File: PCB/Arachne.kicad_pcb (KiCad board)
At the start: 2 copper layers, 100 x 100 mm, 276 parts, among them J201 SW2, J301 SW2, J401 SW2, J501 SW2, J601 SW2, J701 SW2, J801 V_IN, J901 USB_B, J902 PROG_CONN_STM_6p, J903 DBG_UART, M201 Stepper_Motor_bipolar, M301 Stepper_Motor_bipolar, M401 Stepper_Motor_bipolar, M501 Stepper_Motor_bipolar, M601 Stepper_Motor_bipolar, M701 Stepper_Motor_bipolar, Q801 AOD4189, SW101 SW_Push, U101 STM32L452CEUx, U102 WS2818B, U201 L6470_HTSSOP28, U301 L6470_HTSSOP28, U401 L6470_HTSSOP28, U501 L6470_HTSSOP28, U601 L6470_HTSSOP28, U701 L6470_HTSSOP28, U801 ACS712xLCTR-20A, U802 NCP1117-5.0_SOT223, U803 L5973D, U804 NCP1117-3.3_SOT223, U901 USBLC6-2SC6

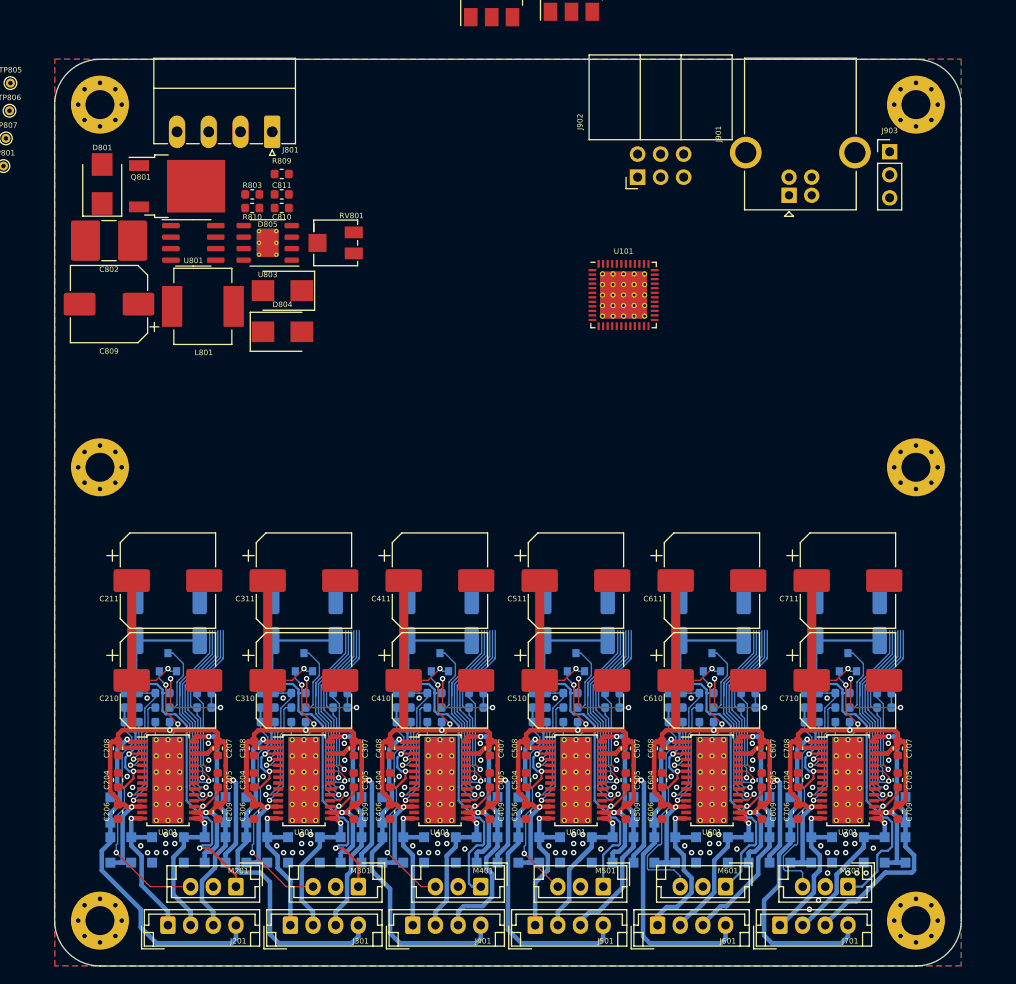
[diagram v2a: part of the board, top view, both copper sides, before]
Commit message: Schema&PCB: shrink board to 80x100mm, remove excessive mounting holes
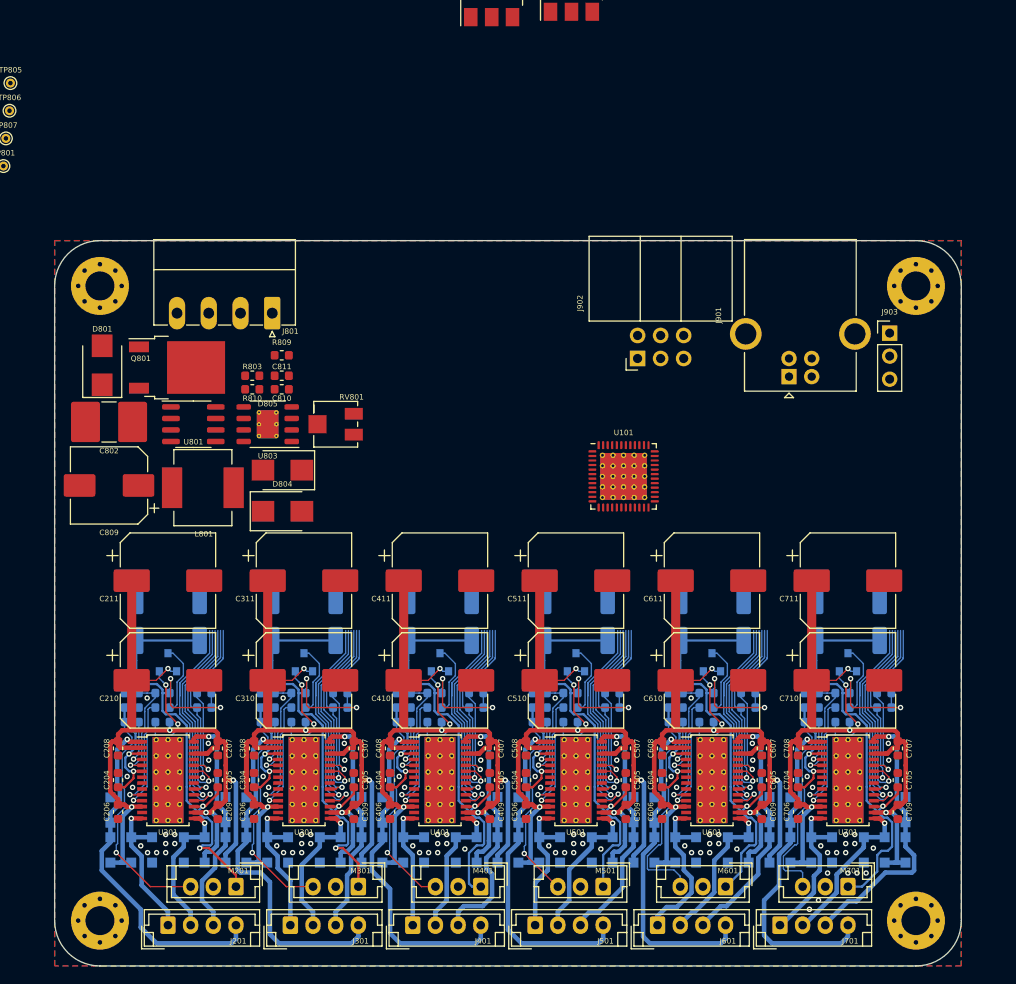
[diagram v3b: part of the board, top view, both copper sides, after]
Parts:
- removed H105, H106: M3, MountingHole:MountingHole_3.2mm_M3_Pad_Via
- moved H101 127.3 mm to (105.0, 145.0)
- moved R809 20.0 mm to (125.0, 82.7)
- moved C802 20.0 mm to (106.0, 90.0)
- moved C809 20.0 mm to (106.0, 97.0)
- moved C810 20.0 mm to (125.0, 86.4)
- moved C811 20.0 mm to (125.0, 84.9)
- moved D801 20.0 mm to (105.2, 83.8)
- moved H102 20.0 mm to (195.0, 75.0)
- moved H103 20.0 mm to (105.0, 75.0)
- moved J801 20.0 mm to (124.0, 78.0)
- moved J901 20.0 mm to (181.0, 85.0)
- moved J902 20.0 mm to (164.3, 83.0)
- moved J903 20.0 mm to (192.1, 80.2)
- moved L801 20.0 mm to (116.3, 97.2)
- moved Q801 20.0 mm to (113.5, 84.0)
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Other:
- board size 100 x 100 mm -> 100 x 80 mm

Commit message: PCB: route bus between drivers, place resistor nets
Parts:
- RN101, RN102, RN103: moved to B.Cu
- moved D104 253.8 mm to (119.0, 115.0), turned to 270 degrees
- moved D102 252.3 mm to (119.0, 122.0), turned to 90 degrees
- moved D103 237.0 mm to (134.0, 115.0), turned to 90 degrees
- moved D101 233.6 mm to (134.0, 122.0), turned to 90 degrees
- moved RN101 229.1 mm to (120.0, 118.0), turned to 270 degrees
- moved RN102 207.9 mm to (150.0, 107.0), turned to 270 degrees
- moved RN103 173.7 mm to (180.0, 107.0), turned to 270 degrees
- moved D105 13.5 mm to (359.5, 52.5), turned to 90 degrees
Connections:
- RN101 pad 5: /BUSY_1 -> /FLAG_2
- RN101 pad 6: /FLAG_1 -> /BUSY_2
- RN101 pad 7: /FLAG_2 -> /FLAG_1
- RN101 pad 8: /BUSY_2 -> /BUSY_1
- RN102 pad 5: /BUSY_3 -> /FLAG_4
- RN102 pad 6: /FLAG_3 -> /BUSY_4
- RN102 pad 7: /FLAG_4 -> /BUSY_3
- RN102 pad 8: /BUSY_4 -> /FLAG_3
- RN103 pad 5: /BUSY_5 -> /FLAG_6
- RN103 pad 6: /FLAG_5 -> /BUSY_6
- RN103 pad 7: /FLAG_6 -> /BUSY_5
- RN103 pad 8: /BUSY_6 -> /FLAG_5
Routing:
- net VMOT: track 546.5 -> 643.0 mm
- net /SPI_MISO: track 154.6 -> 241.3 mm, vias 6 -> 16
- net /SPI_SCK: track 128.5 -> 212.3 mm, vias 6 -> 16
- net /SPI_MOSI: track 128.5 -> 211.3 mm
- net /FLAG_4: track 18.8 -> 15.6 mm
- net /FLAG_2: track 18.8 -> 15.6 mm
- net /FLAG_3: track 18.8 -> 15.7 mm
- net /FLAG_5: track 18.8 -> 15.7 mm
- net /FLAG_1: track 18.8 -> 15.7 mm
- net /FLAG_6: track 18.8 -> 15.8 mm
- net /BUSY_2: track 19.4 -> 16.4 mm
- net /BUSY_4: track 19.4 -> 16.4 mm
- net /BUSY_3: track 19.4 -> 16.4 mm
- net /BUSY_5: track 19.4 -> 16.5 mm
- net /BUSY_6: track 19.4 -> 16.5 mm
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
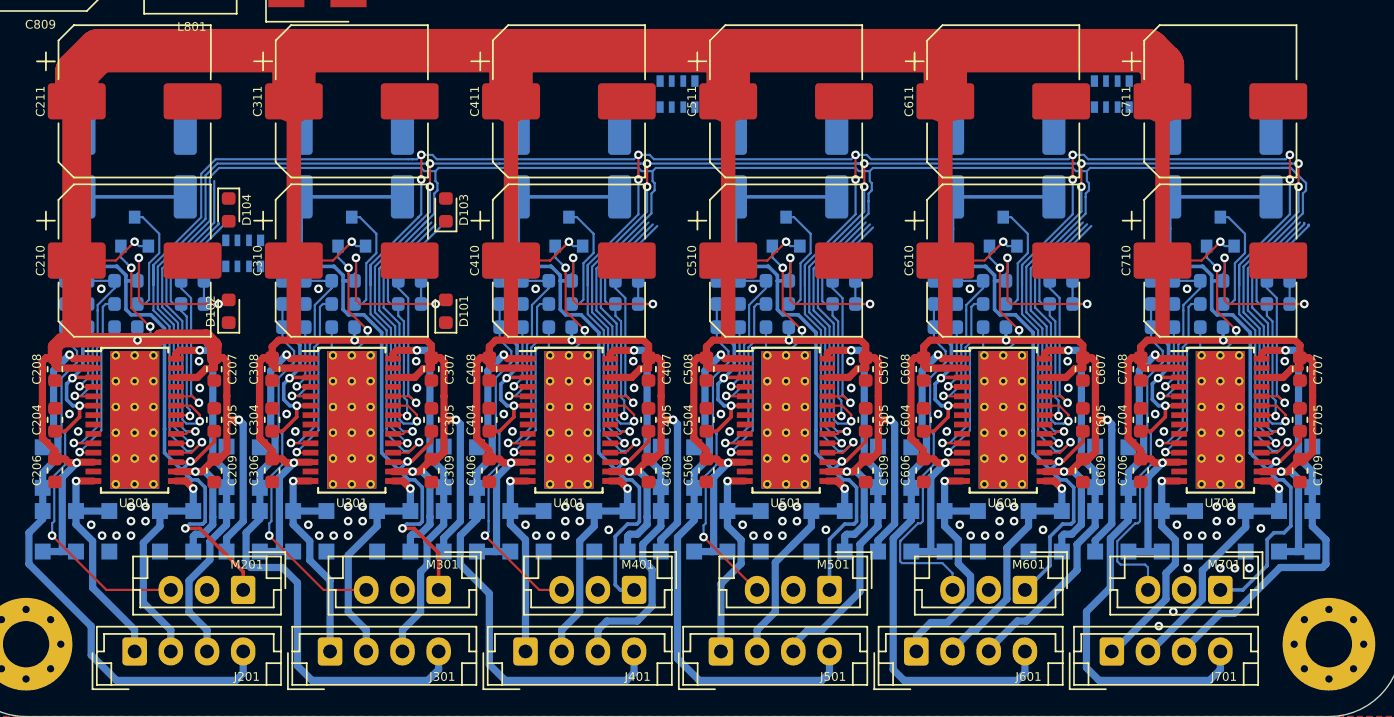
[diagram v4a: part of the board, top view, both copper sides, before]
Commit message: PCB: update VMOT traces to 1 class wider variant
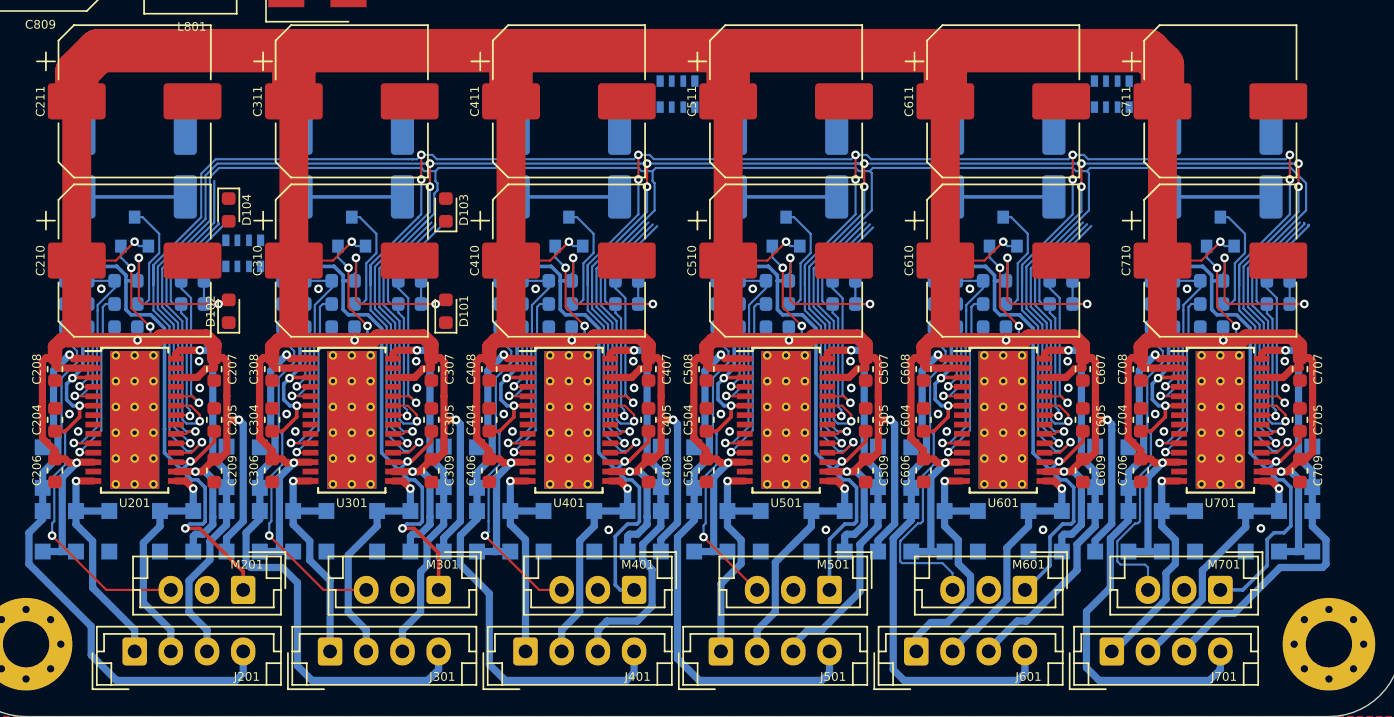
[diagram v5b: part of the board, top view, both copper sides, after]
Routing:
- net +3V3: track 466.6 -> 467.4 mm
- net VMOT: track 643.0 -> 643.9 mm
- net GND: vias 88 -> 34

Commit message: PCB: route current meter, reverse polarity protection, stepdown converter
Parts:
- C802, C804, C805, C810, C811, D803, D804, D805, F801, L901, R801, R802, R804, R805, R808, R809, R810, RV801, U101, U803, U901: moved to B.Cu
- D802: footprint Package_TO_SOT_SMD:SOT-23-6 -> Package_DFN_QFN:ST_UQFN-6L_1.5x1.7mm_Pitch0.5mm; moved to B.Cu
- moved U901 143.0 mm to (182.1, 79.3)
- moved L901 126.6 mm to (182.1, 75.9)
- moved D903 123.6 mm to (204.6, 93.5)
- moved D902 117.2 mm to (209.4, 93.8)
- moved C101 113.5 mm to (225.7, 58.9)
- moved C102 113.5 mm to (225.7, 54.4)
- moved C103 113.5 mm to (230.7, 54.4)
- moved C104 113.5 mm to (220.7, 58.9)
- moved C105 113.5 mm to (230.7, 58.9)
- moved C106 113.5 mm to (230.7, 63.4)
- moved C107 113.5 mm to (220.7, 54.4)
- moved C108 113.5 mm to (225.7, 63.4)
- moved D105 113.5 mm to (248.7, 27.9)
- moved D106 113.5 mm to (251.2, 34.4)
- moved D107 113.5 mm to (251.2, 39.4)
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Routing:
- net Net-(C809-Pad1): track 0.00 -> 36.5 mm, vias 0 -> 4
- net +24V: track 0.00 -> 24.5 mm, vias 0 -> 6
- net /I_MON: track 0.00 -> 23.0 mm, vias 0 -> 1
- net Net-(D805-Pad1): track 0.00 -> 12.1 mm, vias 0 -> 3
- net Net-(R802-Pad1): track 0.00 -> 11.1 mm, vias 0 -> 1
- net Net-(C810-Pad1): track 0.00 -> 10.9 mm
- net Net-(R810-Pad1): track 0.00 -> 10.4 mm
- net Net-(R808-Pad2): track 0.00 -> 9.10 mm
- net Net-(D803-Pad1): track 0.00 -> 8.13 mm
- net /PWR_MON: track 0.00 -> 7.49 mm
- net Net-(D801-Pad2): track 0.00 -> 7.09 mm
- net Net-(J801-Pad3): track 0.00 -> 4.00 mm
- net Net-(C811-Pad2): track 0.00 -> 3.04 mm
- net USB_VCC: track 0.00 -> 2.30 mm
- net Net-(C803-Pad1): track 0.00 -> 2.19 mm
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- added copper zone on B.Cu, net +24V
- added copper zone on F.Cu, net +24V
- added copper zone on F.Cu, net Net-(C809-Pad1)
- added copper zone on F.Cu, net Net-(D801-Pad1)
- added copper zone on B.Cu, net Net-(D805-Pad1)
- added copper zone on F.Cu, net Net-(J801-Pad3)
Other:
- board text added: "GND"
- board text added: "IMON"
- board text added: "INPUT"
- board text added: "IOUT"

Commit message: PCB:
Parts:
- moved D108 131.2 mm to (149.0, 122.0), turned to 270 degrees
- moved D106 130.2 mm to (149.0, 115.0), turned to 270 degrees
- moved D105 126.6 mm to (164.0, 122.0), turned to 270 degrees
- moved D113 120.2 mm to (179.0, 122.0), turned to 270 degrees
- moved D107 115.4 mm to (164.0, 115.0), turned to 270 degrees
- moved D111 97.8 mm to (179.0, 115.0), turned to 270 degrees
- moved D110 96.4 mm to (194.0, 122.0), turned to 270 degrees
- moved D112 92.2 mm to (194.0, 115.0), turned to 270 degrees
- moved R901 67.3 mm to (179.5, 66.7)
- moved R902 67.3 mm to (183.5, 66.7)
- moved D114 31.4 mm to (224.0, 61.0)
- moved R103 25.5 mm to (220.0, 67.0)
- moved C105 25.0 mm to (210.0, 73.0)
- moved C103 24.2 mm to (210.0, 67.0)
- moved C106 24.2 mm to (210.0, 76.0)
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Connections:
- RN101 pad 7: /FLAG_1 -> /BUSY_1
- RN101 pad 8: /BUSY_1 -> /FLAG_1
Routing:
- net +3V3: track 467.4 -> 510.9 mm, vias 32 -> 35
- net /BUSY_6: track 16.5 -> 46.3 mm, vias 1 -> 3
- net /BUSY_4: track 16.4 -> 45.6 mm, vias 1 -> 3
- net /FLAG_6: track 15.8 -> 44.6 mm, vias 1 -> 3
- net /BUSY_2: track 16.4 -> 44.9 mm, vias 1 -> 3
- net /FLAG_2: track 15.6 -> 43.3 mm, vias 1 -> 3
- net /FLAG_4: track 15.6 -> 42.6 mm, vias 1 -> 3
- net Net-(D105-Pad1): track 0.00 -> 20.5 mm, vias 0 -> 1
- net Net-(D101-Pad1): track 0.00 -> 19.7 mm, vias 0 -> 1
- net Net-(D110-Pad1): track 0.00 -> 19.7 mm, vias 0 -> 1
- net /FLAG_5: track 15.7 -> 31.9 mm, vias 1 -> 2
- net /BUSY_5: track 16.5 -> 32.4 mm, vias 1 -> 2
- net Net-(D103-Pad1): track 0.00 -> 15.8 mm, vias 0 -> 1
- net Net-(D107-Pad1): track 0.00 -> 15.0 mm, vias 0 -> 1
- net /BUSY_3: track 16.4 -> 31.2 mm, vias 1 -> 2
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
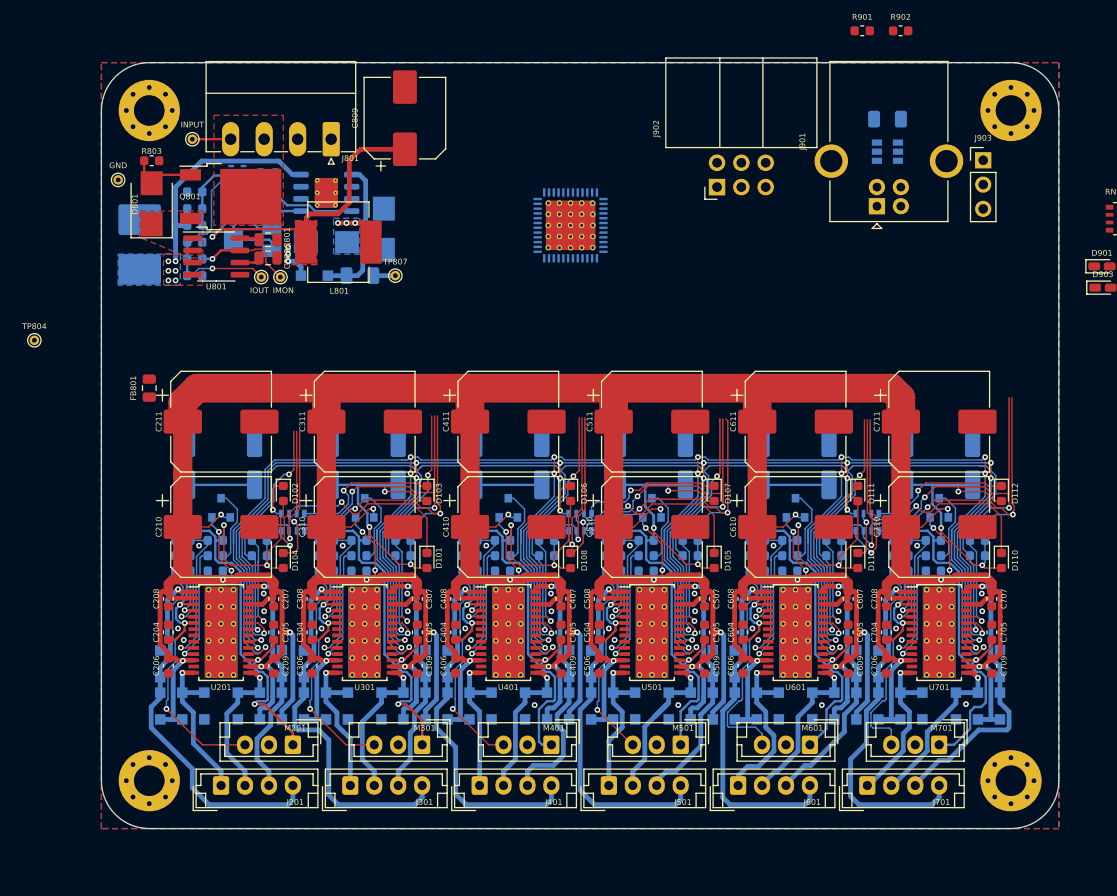
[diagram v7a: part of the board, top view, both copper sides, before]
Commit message: PCB: upgrade power lines for VMOT (3mm -> 5mm), add second ferrite to VMOT
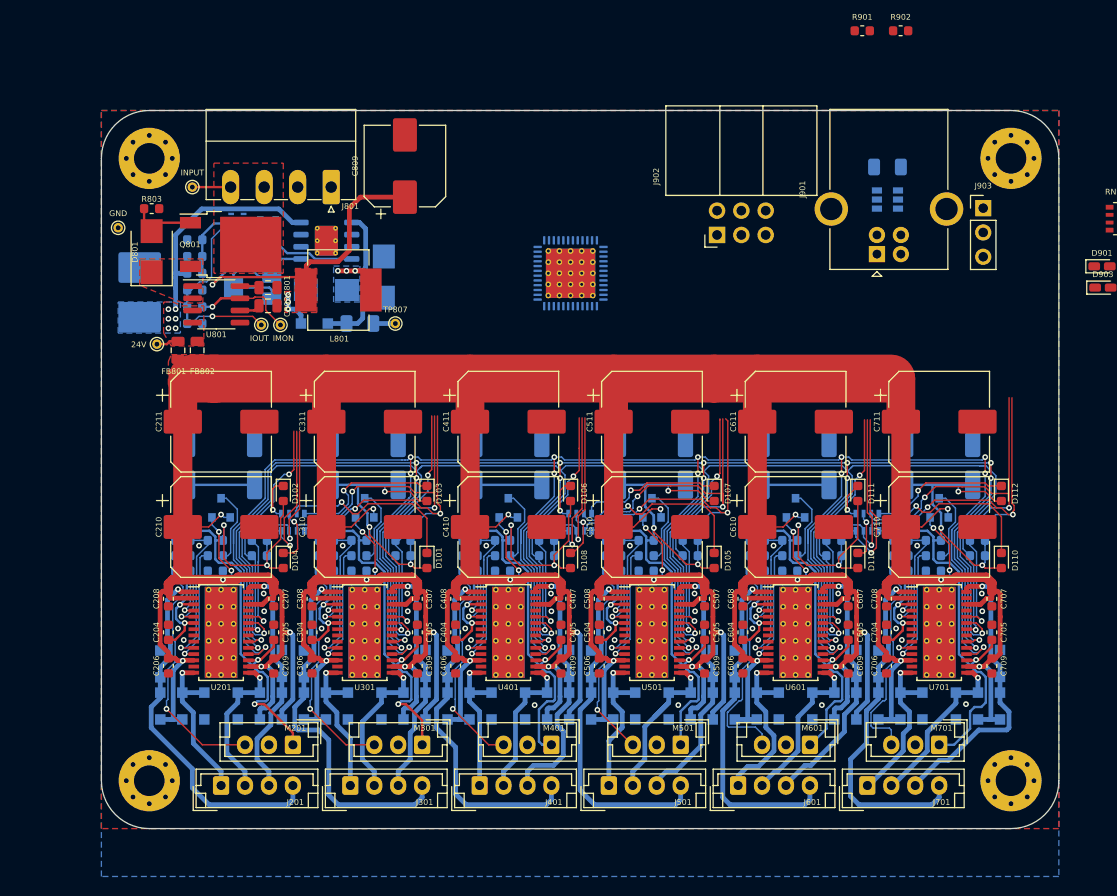
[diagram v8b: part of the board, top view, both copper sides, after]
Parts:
- added FB802: 22R@100MHz, Inductor_SMD:L_0805_2012Metric, F.Cu at (110.0, 100.0)
- moved TP804 12.8 mm to (105.8, 99.4)
- moved C801 5.00 mm to (117.4, 93.5)
- moved C802 5.00 mm to (104.0, 94.0)
- moved C803 5.00 mm to (117.4, 95.4)
- moved C804 5.00 mm to (109.8, 90.2)
- moved C805 5.00 mm to (109.8, 93.8)
- moved C809 5.00 mm to (131.7, 80.8)
- moved C810 5.00 mm to (117.4, 86.5)
- moved C811 5.00 mm to (117.4, 88.2)
- moved D801 5.00 mm to (105.2, 89.8)
- moved D802 5.00 mm to (114.2, 86.3)
- moved D803 5.00 mm to (122.2, 97.2)
- moved D804 5.00 mm to (129.5, 92.4)
- moved D805 5.00 mm to (123.5, 93.8)
- moved F801 5.00 mm to (127.0, 97.2)
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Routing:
- net VMOT: track 646.8 -> 651.7 mm
- net +24V: track 24.5 -> 26.9 mm
- added copper zone on F.Cu, net VMOT
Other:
- board size 100 x 80 mm -> 100 x 75 mm
- board text added: "24V"
